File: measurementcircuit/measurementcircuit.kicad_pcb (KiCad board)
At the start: 2 copper layers, 174.5 x 220 mm, 81 parts, among them J1 Conn_01x02, J10 Conn_01x02, J11 Conn_01x02, J12 Conn_01x02, J13 250-108/000-006, J15 Conn_01x02, J16 Conn_01x02, J17 250-116/000-012, J18 2604-3102, J19 2604-3102, J2 Conn_01x02, J20 2604-3102, J21 Conn_01x02, J22 Conn_01x02, J23 Conn_01x02, J24 Conn_01x02, J25 Conn_01x02, J26 Conn_01x02, J27 Conn_01x02, J28 Conn_01x02, J29 Conn_01x02, J3 2604-3102, J30 Conn_01x02, J31 Conn_01x02, J32 Conn_01x02, J33 Conn_01x02, J34 Conn_01x02, J35 Conn_01x02, J36 Conn_01x02, J37 Conn_01x02, J38 Conn_01x02, J39 Conn_01x02, J4 2604-3102, J40 Conn_01x02, J41 Conn_01x02, J42 Conn_01x02, J5 2604-3102, J6 2604-3102, J7 2604-3102, J8 Conn_01x02, J9 Conn_01x02

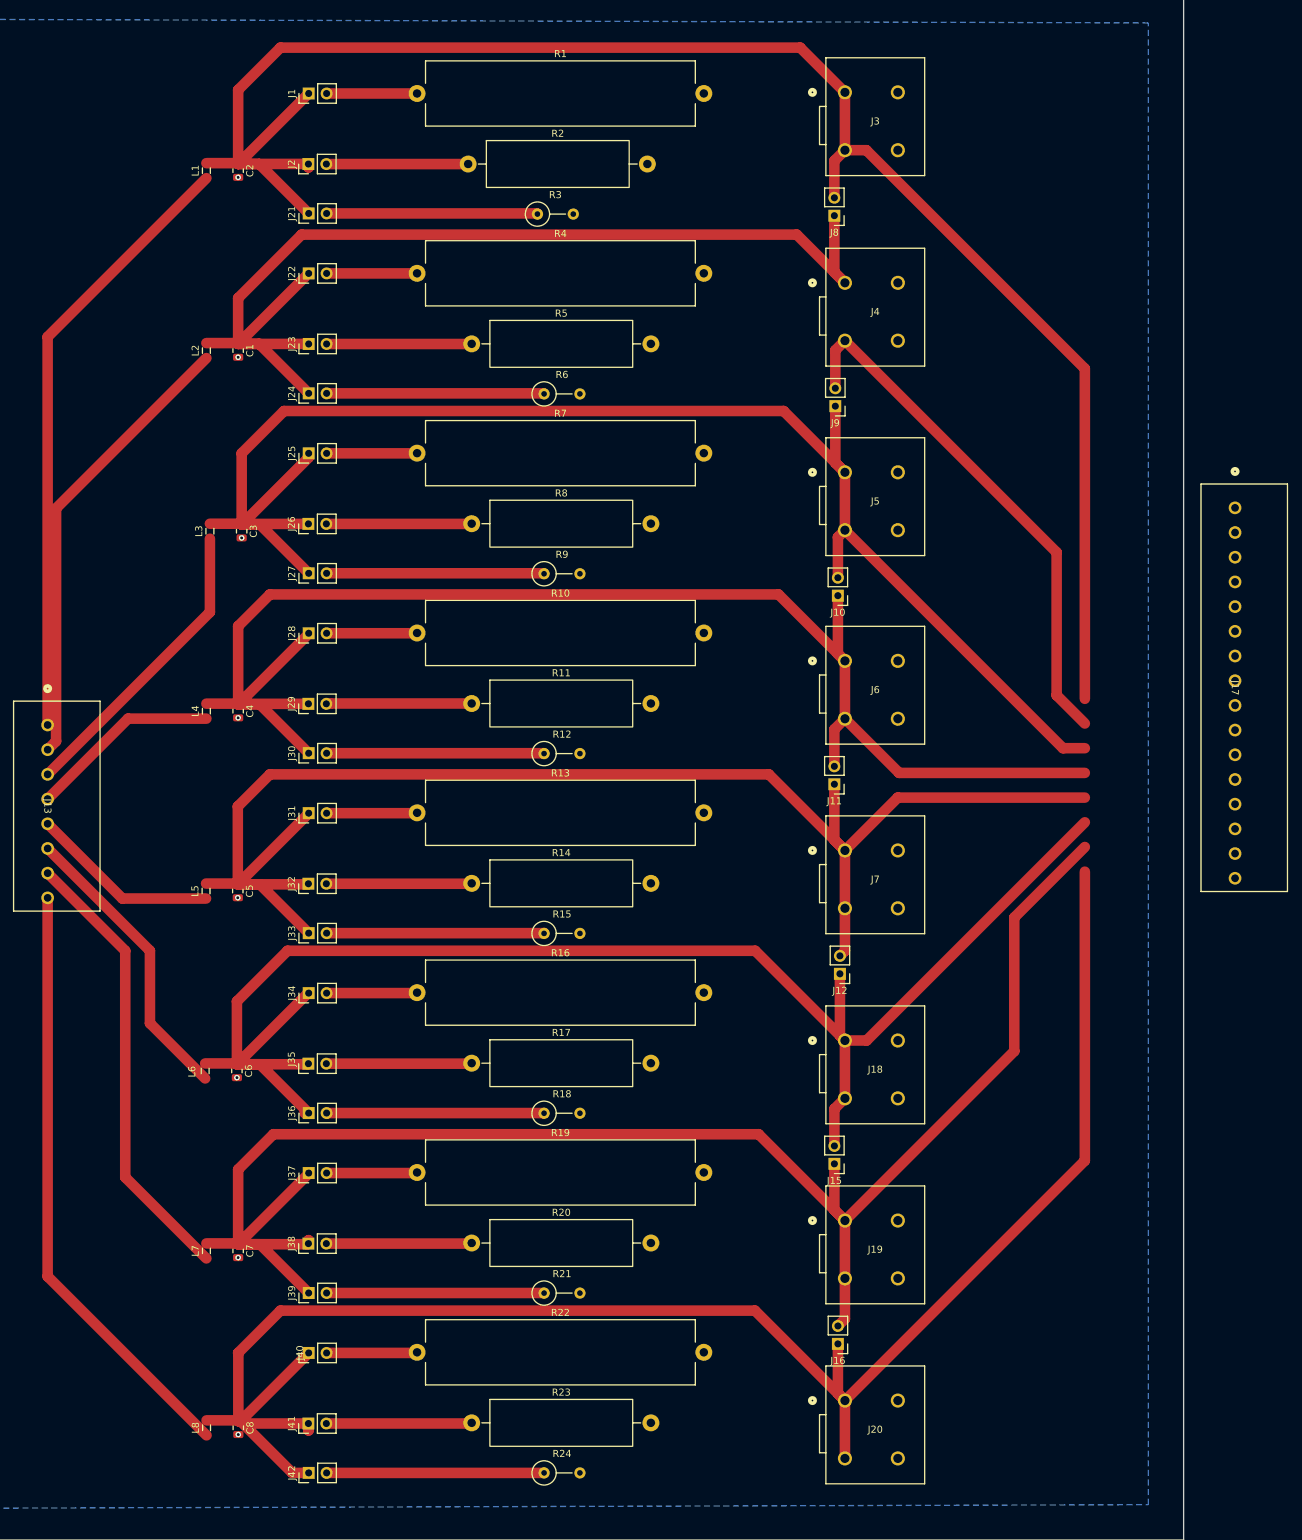
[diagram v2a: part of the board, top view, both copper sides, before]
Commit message: Fix traces after rearrangement of measurement schematic
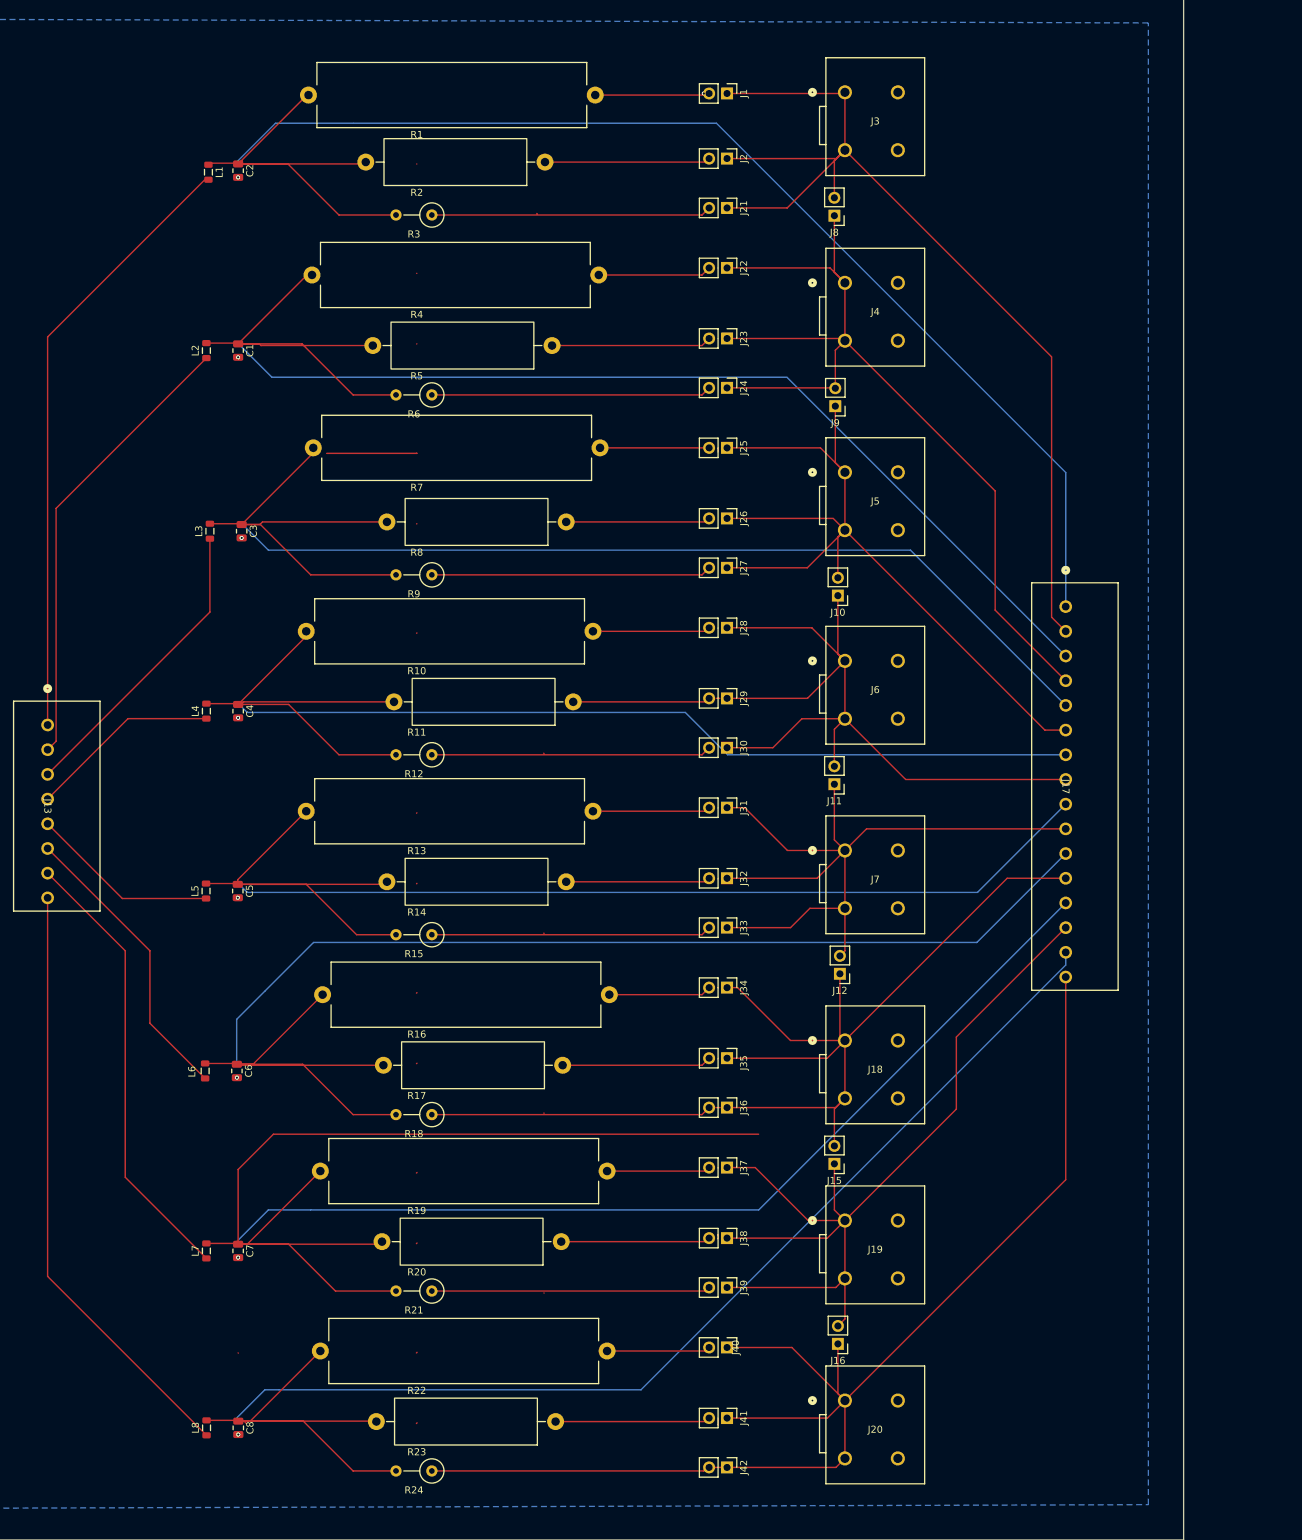
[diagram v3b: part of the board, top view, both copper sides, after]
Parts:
- moved J2 59.3 mm to (-85.5, -55.0), turned to -90 degrees
- moved J26 59.3 mm to (-85.5, -4.00), turned to -90 degrees
- moved J29 59.3 mm to (-85.5, 21.5), turned to -90 degrees
- moved J32 59.3 mm to (-85.5, 47.0), turned to -90 degrees
- moved J35 59.3 mm to (-85.5, 72.5), turned to -90 degrees
- moved J38 59.3 mm to (-85.5, 98.0), turned to -90 degrees
- moved J41 59.3 mm to (-85.5, 123.5), turned to -90 degrees
- moved J21 59.3 mm to (-85.5, -48.0), turned to -90 degrees
- moved J22 59.3 mm to (-85.5, -39.5), turned to -90 degrees
- moved J23 59.3 mm to (-85.5, -29.5), turned to -90 degrees
- moved J24 59.3 mm to (-85.5, -22.5), turned to -90 degrees
- moved J25 59.3 mm to (-85.5, -14.0), turned to -90 degrees
- moved J27 59.3 mm to (-85.5, 3.00), turned to -90 degrees
- moved J28 59.3 mm to (-85.5, 11.5), turned to -90 degrees
- moved J30 59.3 mm to (-85.5, 28.5), turned to -90 degrees
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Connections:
- J18 pad 3: Net-(J18-2_1) -> GND
- J18 pad 4: Net-(J18-2_1) -> GND
- J19 pad 3: Net-(J19-2_1) -> GND
- J19 pad 4: Net-(J19-2_1) -> GND
- J20 pad 3: Net-(J20-2_1) -> GND
- J20 pad 4: Net-(J20-2_1) -> GND
- J3 pad 3: Net-(J3-2_1) -> GND
- J3 pad 4: Net-(J3-2_1) -> GND
- J4 pad 3: Net-(J4-2_1) -> GND
- J4 pad 4: Net-(J4-2_1) -> GND
- J5 pad 3: Net-(J5-2_1) -> GND
- J5 pad 4: Net-(J5-2_1) -> GND
- J6 pad 3: Net-(J6-2_1) -> GND
- J6 pad 4: Net-(J6-2_1) -> GND
- J7 pad 3: Net-(J7-2_1) -> GND
- J7 pad 4: Net-(J7-2_1) -> GND
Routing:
- net Net-(C7-Pad1): track 0.00 -> 290.1 mm, vias 3 -> 0
- net Net-(C2-Pad1): track 0.00 -> 221.6 mm, vias 3 -> 0
- net Net-(C8-Pad1): track 0.00 -> 212.5 mm, vias 3 -> 0
- net Net-(C6-Pad1): track 0.00 -> 200.4 mm, vias 3 -> 0
- net Net-(C3-Pad1): track 0.00 -> 193.5 mm, vias 3 -> 0
- net Net-(C5-Pad1): track 0.00 -> 188.9 mm, vias 3 -> 0
- net Net-(J22-Pin_1): track 226.4 -> 336.2 mm, vias 3 -> 0
- net Net-(J16-Pin_1): track 251.4 -> 147.8 mm
- net Net-(J15-Pin_1): track 236.9 -> 134.0 mm
- net Net-(J1-Pin_1): track 252.8 -> 151.3 mm
- net Net-(J12-Pin_1): track 218.2 -> 121.8 mm
- net Net-(J10-Pin_1): track 206.9 -> 303.3 mm, vias 3 -> 0
- net Net-(J11-Pin_1): track 207.5 -> 113.4 mm
- net Net-(J10-Pin_2): track 214.3 -> 123.4 mm
- net Net-(J25-Pin_2): track 12.8 -> 28.3 mm
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
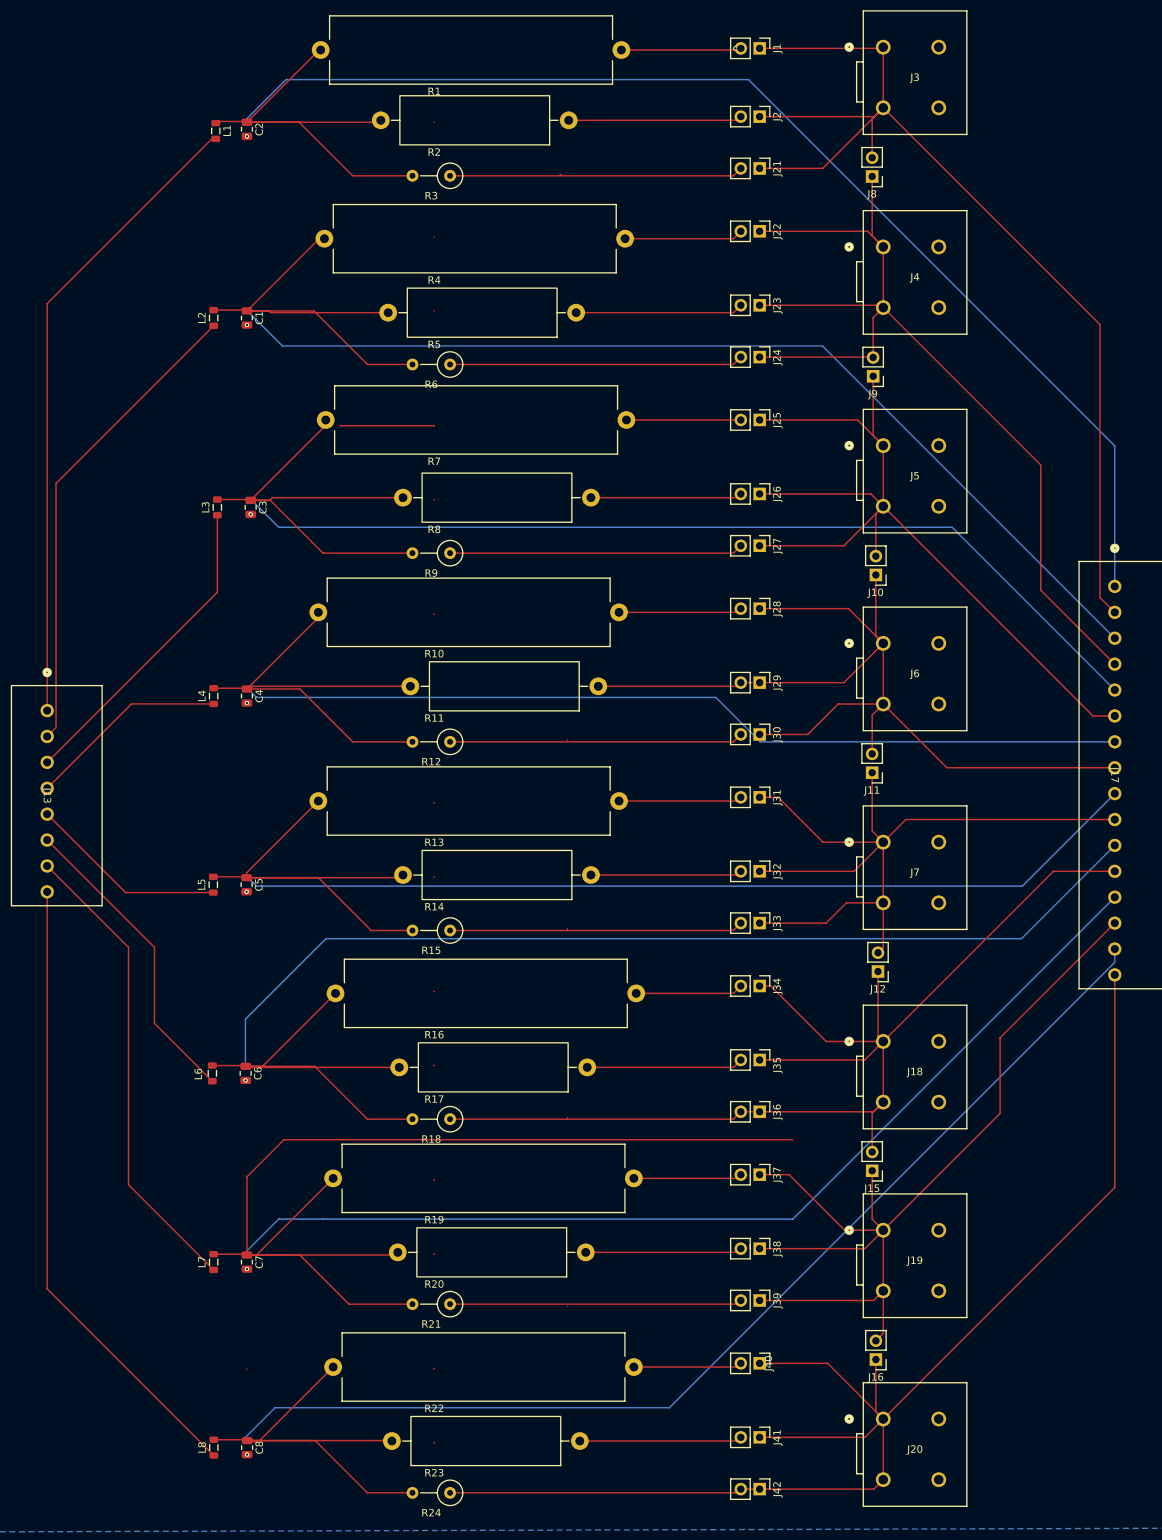
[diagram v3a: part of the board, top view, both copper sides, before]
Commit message: cleanup for CDR
traces wider, etc
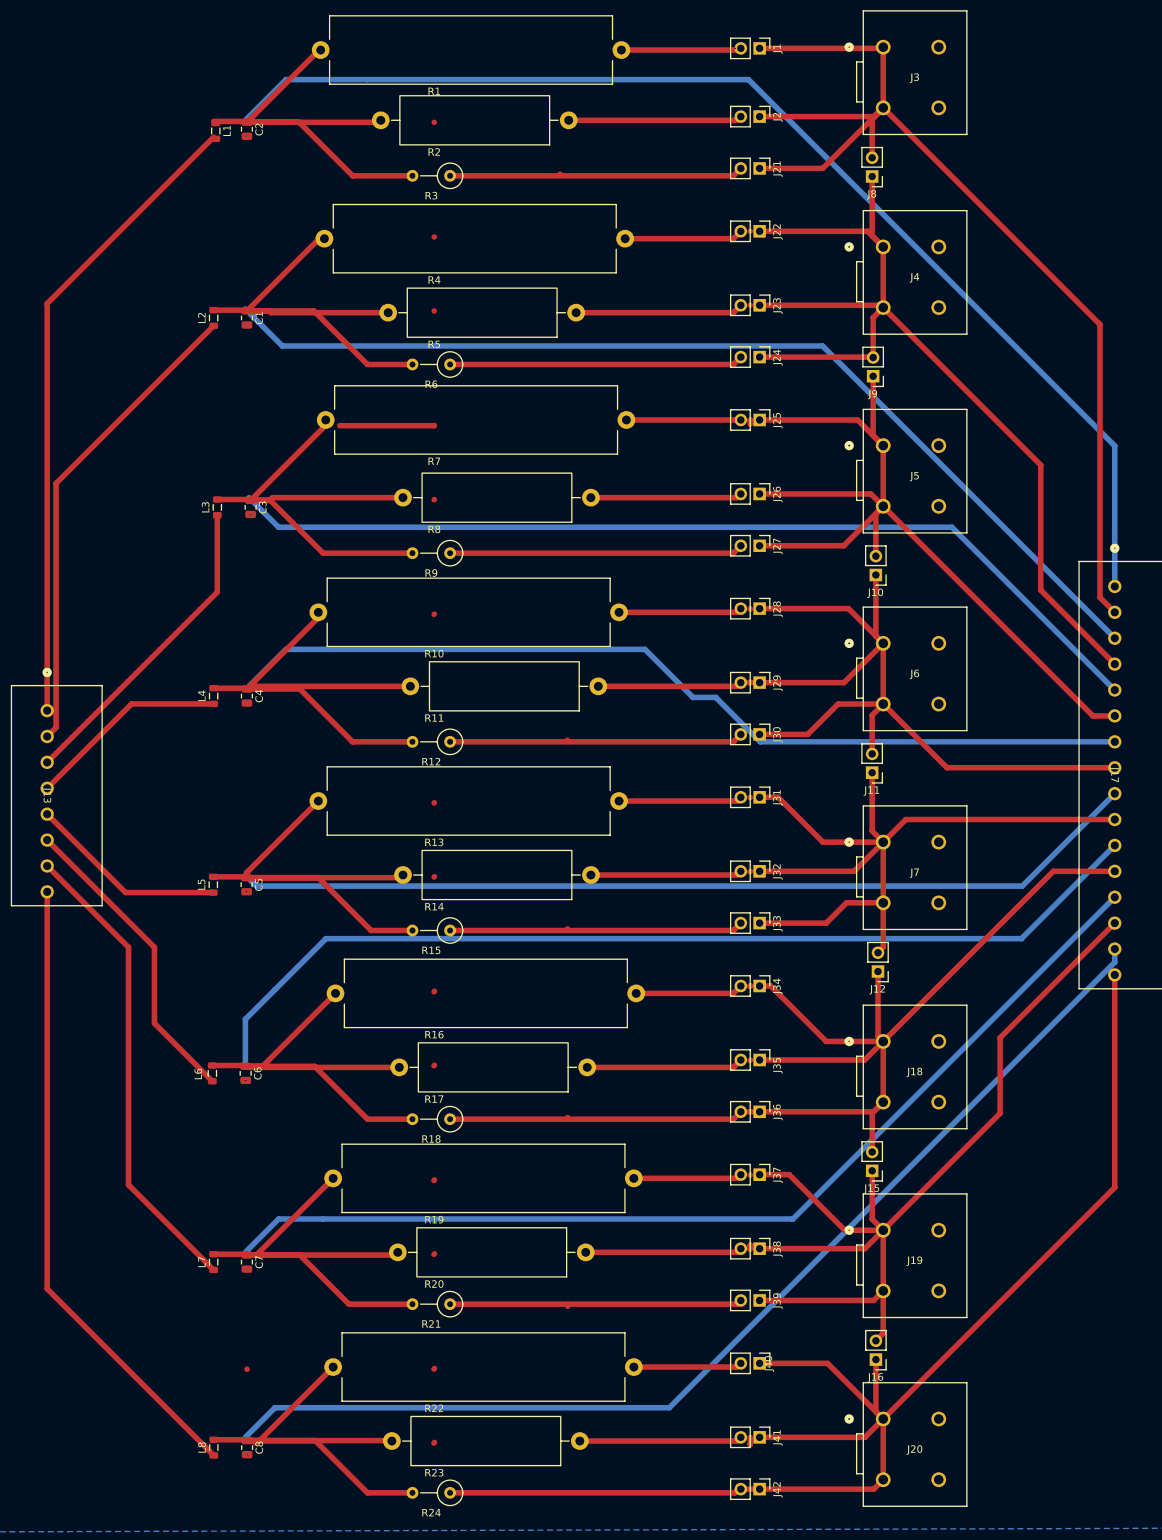
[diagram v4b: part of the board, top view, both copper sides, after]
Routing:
- net Net-(C7-Pad1): track 290.1 -> 203.6 mm
- net Net-(J10-Pin_1): track 303.3 -> 306.9 mm
- net Net-(J38-Pin_2): track 21.2 -> 21.8 mm
- net Net-(J15-Pin_1): track 134.0 -> 133.4 mm

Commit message: Edit random dots out
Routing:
- net Net-(J25-Pin_2): track 28.3 -> 15.5 mm
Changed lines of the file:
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@@
-	)
-	(segment
-		(start -129.477825 -54.222761)
-		(end -129.473477 -54.227109)
-		(width 0.75)
-		(layer "F.Cu")
-		(net 2)
 	)
 	(segment
@@
 	)
 	(segment
-		(start -129.490869 -3.222761)
-		(end -129.460434 -3.253196)
-		(width 0.75)
-		(layer "F.Cu")
-		(net 10)
-	)
-	(segment
 		(start -91.41124 23.501)
 		(end -94.499 23.501)
@@
 	)
 	(segment
-		(start -129.482173 -38.722761)
-		(end -129.46913 -38.735804)
-		(width 0.75)
-		(layer "F.Cu")
-		(net 21)
-	)
-	(segment
 		(start -103.68 -38.5)
 		(end -89.04 -38.5)
@@
 	)
 	(segment
-		(start -142.249999 -13.222761)
-		(end -129.456086 -13.222761)
-		(width 0.75)
-		(layer "F.Cu")
-		(net 24)
-	)
-	(segment
 		(start -103.5 -14)
 		(end -88.04 -14)
@@
 	)
 	(segment
-		(start -129.488695 -13.222761)
-		(end -129.462608 -13.248848)
-		(width 0.75)
-		(layer "F.Cu")
-		(net 24)
-	)
-	(segment
 		(start -108.3 -3.5)
 		(end -88.54 -3.5)
@@
 	)
 	(segment
-		(start -129.495216 12.277239)
-		(end -129.456086 12.238109)
-		(width 0.75)
-		(layer "F.Cu")
-		(net 27)
-	)
-	(segment
 		(start -88.54 12)
 		(end -88.04 11.5)
@@
 	)
 	(segment
-		(start -111.482173 29.277239)
-		(end -111.429999 29.329413)
-		(width 0.75)
-		(layer "F.Cu")
-		(net 29)
-	)
-	(segment
-		(start -129.501738 37.777239)
-		(end -129.449564 37.725065)
-		(width 0.75)
-		(layer "F.Cu")
-		(net 30)
-	)
-	(segment
 		(start -104.5 37.5)
 		(end -88.54 37.5)
@@
 	)
 	(segment
-		(start -111.469129 54.777239)
-		(end -111.429999 54.816369)
-		(width 0.75)
-		(layer "F.Cu")
-		(net 32)
-	)
-	(segment
 		(start -127.335651 55)
 		(end -89.04 55)
@@
 	)
 	(segment
-		(start -129.50826 63.277239)
-		(end -129.443043 63.212022)
-		(width 0.75)
-		(layer "F.Cu")
-		(net 33)
-	)
-	(segment
 		(start -108.8 73.5)
 		(end -89.04 73.5)
@@
 	)
 	(segment
-		(start -129.514782 88.777239)
-		(end -129.436521 88.698978)
-		(width 0.75)
-		(layer "F.Cu")
-		(net 36)
-	)
-	(segment
 		(start -86.81875 98.0875)
 		(end -86.73125 98)
@@
 	)
 	(segment
-		(start -129.521303 114.277239)
-		(end -129.429999 114.185935)
-		(width 0.75)
-		(layer "F.Cu")
-		(net 39)
-	)
-	(segment
 		(start -88.54 114)
 		(end -88.04 113.5)
@@
 	)
 	(segment
-		(start -129.523477 124.277239)
-		(end -129.427825 124.181587)
-		(width 0.75)
-		(layer "F.Cu")
-		(net 40)
-	)
-	(segment
 		(start -88.54 124)
 		(end -88.04 123.5)
@@
 	)
 	(segment
-		(start -129.484347 -28.722761)
-		(end -129.466956 -28.740152)
-		(width 0.75)
-		(layer "F.Cu")
-		(net 43)
-	)
-	(segment
 		(start -158.789999 -3.247761)
 		(end -154.402499 -3.247761)
@@
 	)
 	(segment
-		(start -129.503912 47.777239)
-		(end -129.44739 47.720717)
-		(width 0.75)
-		(layer "F.Cu")
-		(net 45)
-	)
-	(segment
 		(start -145.640123 73.359877)
 		(end -138.5 80.5)
@@
 	)
 	(segment
-		(start -129.510434 73.277239)
-		(end -129.440869 73.207674)
-		(width 0.75)
-		(layer "F.Cu")
-		(net 46)
-	)
-	(segment
 		(start -147.635261 98.864739)
 		(end -141 105.5)
@@
 	)
 	(segment
-		(start -129.516956 98.777239)
-		(end -129.434347 98.69463)
-		(width 0.75)
-		(layer "F.Cu")
-		(net 47)
-	)
-	(segment
 		(start -154.878907 123.826955)
 		(end -154.766407 123.939455)
 		(width 0.75)
 		(layer "F.Cu")
-		(net 47)
-	)
-	(segment
-		(start -154.766407 114.300831)
-		(end -154.789999 114.277239)
-		(width 0.75)
-		(layer "F.Cu")
